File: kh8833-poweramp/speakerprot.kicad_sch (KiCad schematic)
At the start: 17 parts

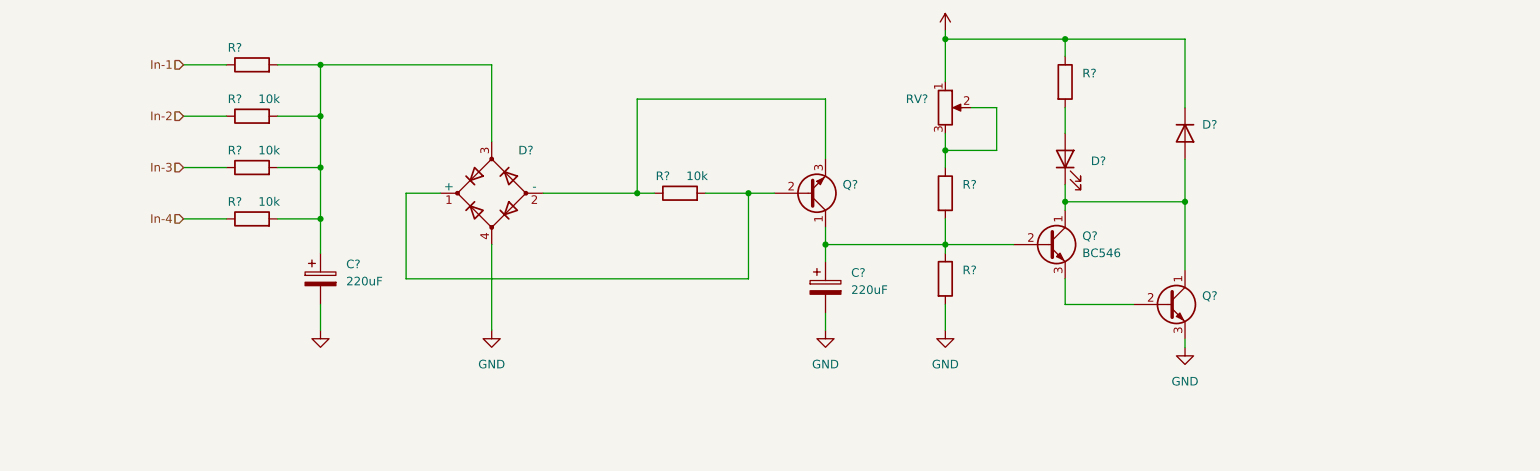
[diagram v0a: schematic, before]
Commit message: Add speaker prot - v1.0
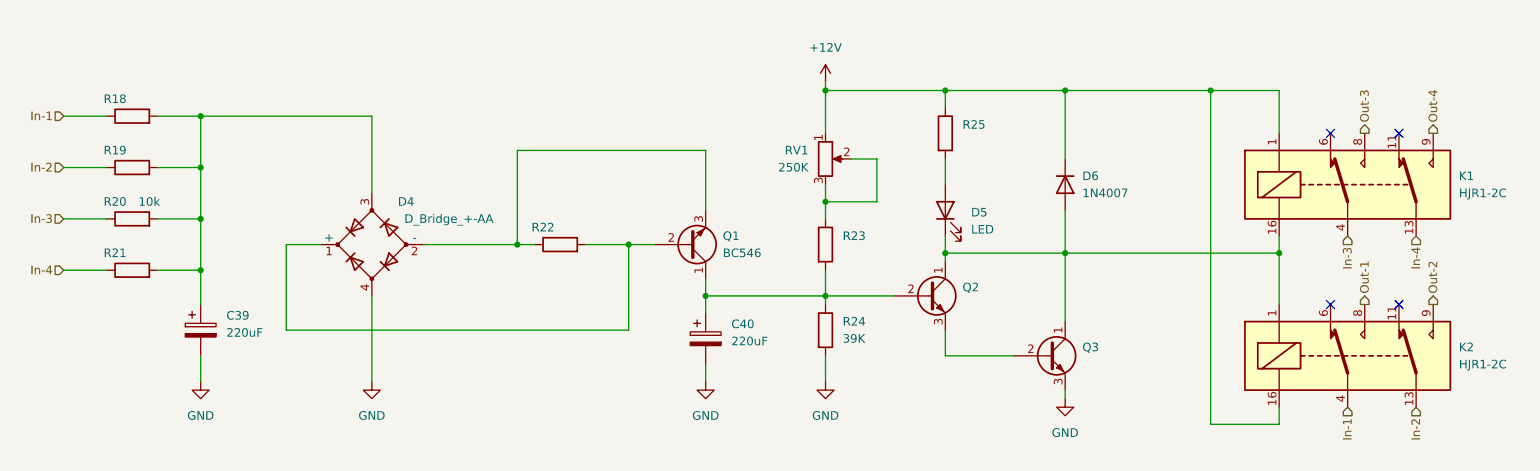
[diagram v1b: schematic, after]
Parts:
- added K1, K2: HJR1-2C, Relay_THT:Relay_DPDT_Omron_G5V-2, symbol Relay:G5V-2
- D4: renamed from D?; value (none) -> D_Bridge_+-AA; footprint (none) -> Diode_THT:Diode_Bridge_Round_D9.0mm
- D5: renamed from D?; value (none) -> LED; footprint (none) -> LED_THT:LED_D5.0mm
- D6: renamed from D?; value (none) -> 1N4007; footprint (none) -> Diode_THT:D_DO-41_SOD81_P10.16mm_Horizontal
- Q1: renamed from Q?; value (none) -> BC546; footprint (none) -> Package_TO_SOT_THT:TO-92L_Inline_Wide
- Q2: renamed from Q?; value BC546 -> (none); footprint Package_TO_SOT_THT:TO-92L_Inline_Wide -> (none)
- R18, R23, R25: renamed from R?; footprint Resistor_THT:R_Axial_DIN0207_L6.3mm_D2.5mm_P10.16mm_Horizontal -> (none)
- R19, R21, R22: renamed from R?; value 10k -> (none); footprint Resistor_THT:R_Axial_DIN0207_L6.3mm_D2.5mm_P10.16mm_Horizontal -> (none)
- R24: renamed from R?; value (none) -> 39K
- RV1: renamed from RV?; value (none) -> 250K; footprint (none) -> Potentiometer_THT:Potentiometer_Bourns_3296W_Vertical
- gave numbers to parts that had none: 4
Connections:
- net +12V: now also K1.1, K2.16
- net In-1: now also K2.4
- net In-2: now also K2.13
- net In-3: now also K1.4
- net In-4: now also K1.13
- net at D5.1 (K), D6.2 (A), Q2.1 (C)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: now also K1.16, K2.1
- new net Out-1: K2.8
- new net Out-2: K2.9
- new net Out-3: K1.8
- new net Out-4: K1.9
- no-connect marks 0 -> 4
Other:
- moved on the sheet: C39, C40, D4, D5, D6, Q1, Q2, Q3, R18, R19, R20, R21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
